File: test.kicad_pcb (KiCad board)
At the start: 2 copper layers, 47 x 92.7 mm, 6 parts, among them J1 Conn_01x32_Female, J2 Conn_01x32_Female, J3 DB9_Male, J4 Conn_01x32_Female, J5 Conn_01x32_Female, U1 MCP2551-I-SN

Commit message: Update db9 position for CAD
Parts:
- J3: moved to B.Cu
- moved J3 22.1 mm to (88.3, 136.0), turned to 180 degrees
- moved J4 11.8 mm to (106.8, 62.2)
- moved J5 11.8 mm to (109.3, 62.2)
- moved U1 6.36 mm to (82.7, 127.2), turned to 180 degrees
- moved J1 2.58 mm to (56.1, 62.2)
- moved J2 2.58 mm to (58.6, 62.2)
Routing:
- net PB12: track 218.9 -> 26.0 mm
- net canH: track 26.8 -> 14.9 mm
- net canL: track 22.6 -> 13.8 mm
- net PB13: track 32.3 -> 24.0 mm
- net GND_STM: track 37.1 -> 40.4 mm
- net +5V_STM: track 79.1 -> 77.7 mm
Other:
- board size 47 x 92.7 mm -> 56.7 x 82.3 mm

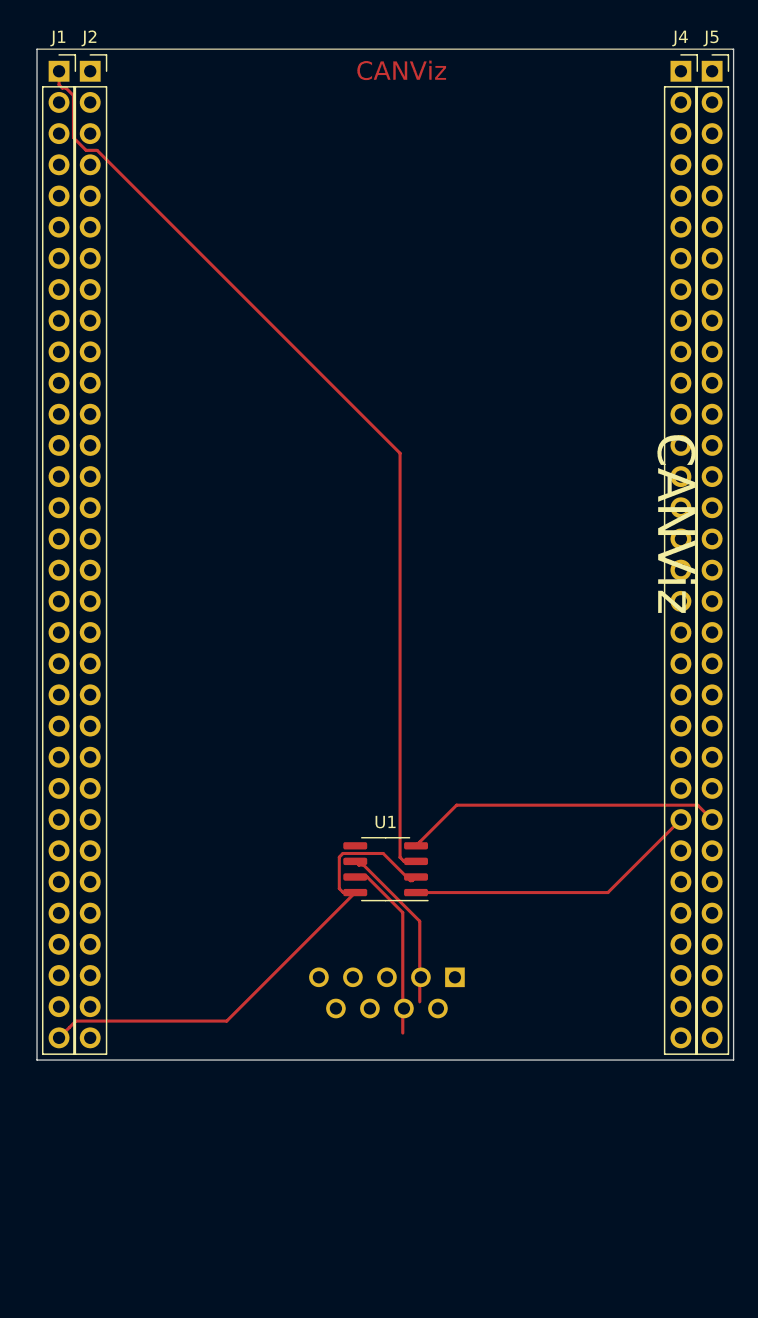
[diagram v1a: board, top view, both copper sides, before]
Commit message: use less pin sockets
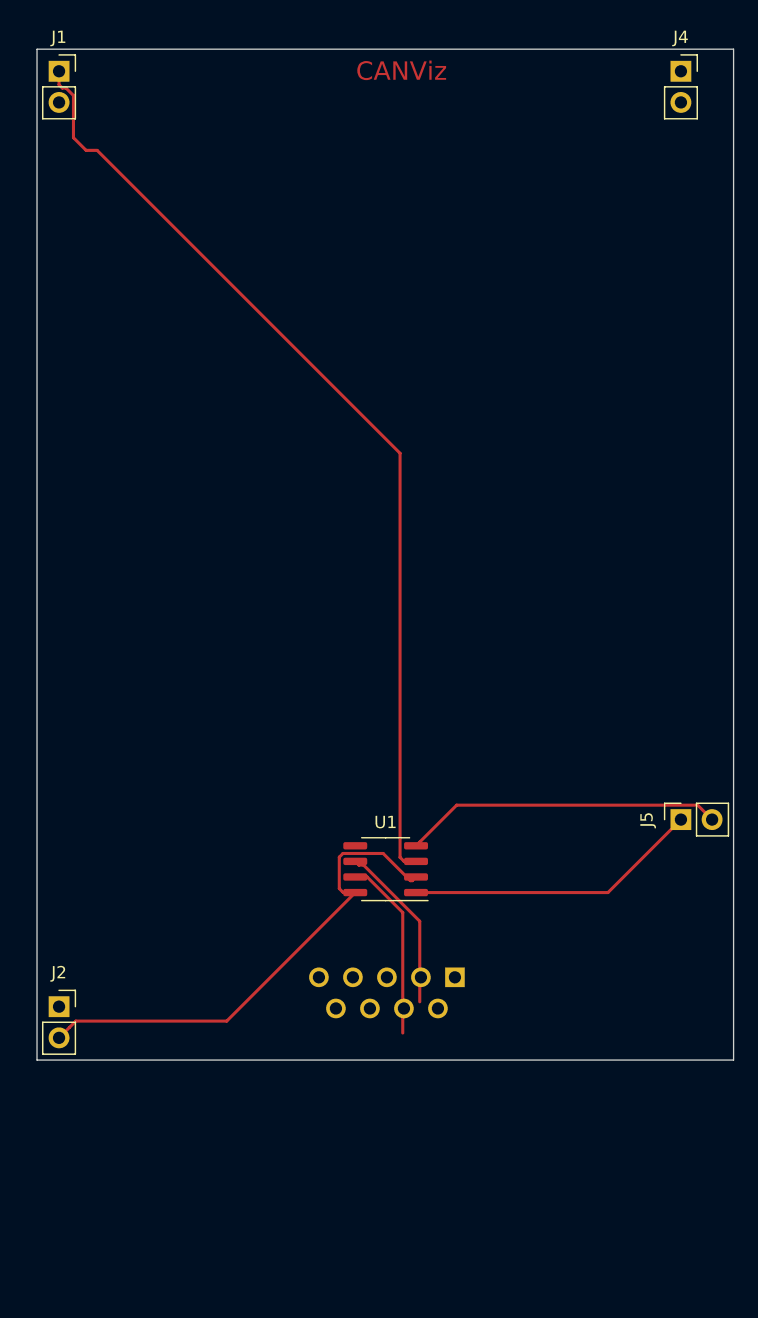
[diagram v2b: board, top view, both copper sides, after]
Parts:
- J1, J2, J4, J5: value Conn_01x32_Female -> Conn_01x02_Female; footprint Connector_PinSocket_2.54mm:PinSocket_1x32_P2.54mm_Vertical -> Connector_PinSocket_2.54mm:PinSocket_1x02_P2.54mm_Vertical
- moved J2 76.2 mm to (56.1, 138.4)
- moved J5 61.0 mm to (106.8, 123.2), turned to 90 degrees
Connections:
- J2 pad 2: Net-(J2-Pad2) -> GND_STM
- J5 pad 1: Net-(J5-Pad1) -> PB13
- J5 pad 2: Net-(J5-Pad2) -> PB12

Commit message: Gerbers and BOM files
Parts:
- moved J4 2.60 mm to (109.4, 62.2)
- moved J5 0.06 mm to (106.8, 123.2)
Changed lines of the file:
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@@
     (thickness 1.6)
     (drawings 7)
-    (tracks 38)
+    (tracks 32)
     (zones 0)
     (modules 6)
@@
       (outputformat 1)
       (mirror false)
-      (drillshape 1)
+      (drillshape 0)
       (scaleselection 1)
-      (outputdirectory ""))
+      (outputdirectory "gerbers/"))
   )
   (net 0 "")
@@
   )
   (module Connector_PinSocket_2.54mm:PinSocket_1x02_P2.54mm_Vertical (layer F.Cu)
-    (at 106.76 62.2)
+    (at 109.36 62.2)
     (descr "Through hole straight socket strip, 1x02, 2.54mm pitch, single row (from Kicad 4.0.7), script generated")
     (tags "Through hole socket strip THT 1x02 2.54mm single row")
@@
   )
   (module Connector_PinSocket_2.54mm:PinSocket_1x02_P2.54mm_Vertical (layer F.Cu)
-    (at 106.76 123.16 90)
+    (at 106.82 123.16 90)
     (descr "Through hole straight socket strip, 1x02, 2.54mm pitch, single row (from Kicad 4.0.7), script generated")
     (tags "Through hole socket strip THT 1x02 2.54mm single row")
@@
   (gr_line (start 111.0488 142.748) (end 111.0488 60.4012) (layer Edge.Cuts) (width 0.05))
   (gr_line (start 54.3052 142.748) (end 111.0488 142.748) (layer Edge.Cuts) (width 0.05))
-  (segment (start 84.2045 126.565) (end 85.1795 126.565) (width 0.25) (layer F.Cu) (net 1))
-  (segment (start 83.87949 126.23999) (end 84.2045 126.565) (width 0.25) (layer F.Cu) (net 1))
-  (segment (start 59.204001 68.644999) (end 83.87949 93.320488) (width 0.25) (layer F.Cu) (net 1))
-  (segment (start 58.307199 68.644999) (end 59.204001 68.644999) (width 0.25) (layer F.Cu) (net 1))
-  (segment (start 57.275001 64.175999) (end 57.275001 67.612801) (width 0.25) (layer F.Cu) (net 1))
-  (segment (start 56.664001 63.564999) (end 57.275001 64.175999) (width 0.25) (layer F.Cu) (net 1))
-  (segment (start 56.364999 63.564999) (end 56.664001 63.564999) (width 0.25) (layer F.Cu) (net 1))
-  (segment (start 57.275001 67.612801) (end 58.307199 68.644999) (width 0.25) (layer F.Cu) (net 1))
-  (segment (start 56.1 63.3) (end 56.364999 63.564999) (width 0.25) (layer F.Cu) (net 1))
-  (segment (start 83.87949 93.320488) (end 83.87949 126.23999) (width 0.25) (layer F.Cu) (net 1))
-  (segment (start 56.1 62.2) (end 56.1 63.3) (width 0.25) (layer F.Cu) (net 1))
+  (segment (start 57.2 62.2) (end 56.1 62.2) (width 0.25) (layer F.Cu) (net 1))
+  (segment (start 57.275001 62.275001) (end 57.2 62.2) (width 0.25) (layer F.Cu) (net 1))
+  (segment (start 57.275001 99.635501) (end 57.275001 62.275001) (width 0.25) (layer F.Cu) (net 1))
+  (segment (start 84.2045 126.565) (end 57.275001 99.635501) (width 0.25) (layer F.Cu) (net 1))
+  (segment (start 85.1795 126.565) (end 84.2045 126.565) (width 0.25) (layer F.Cu) (net 1))
   (segment (start 78.92949 128.77999) (end 79.2545 129.105) (width 0.25) (layer F.Cu) (net 3))
   (segment (start 78.92949 126.218242) (end 78.92949 128.77999) (width 0.25) (layer F.Cu) (net 3))

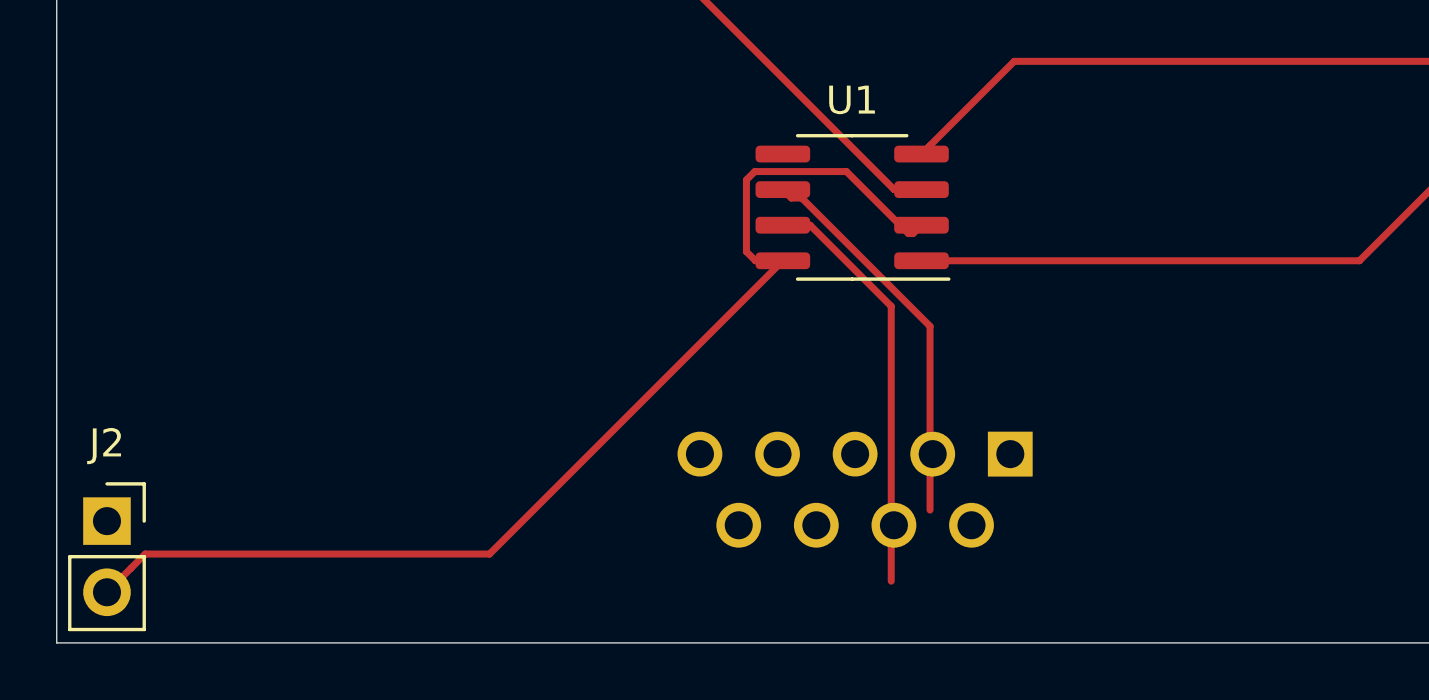
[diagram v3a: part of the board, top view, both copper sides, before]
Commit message: housed db9
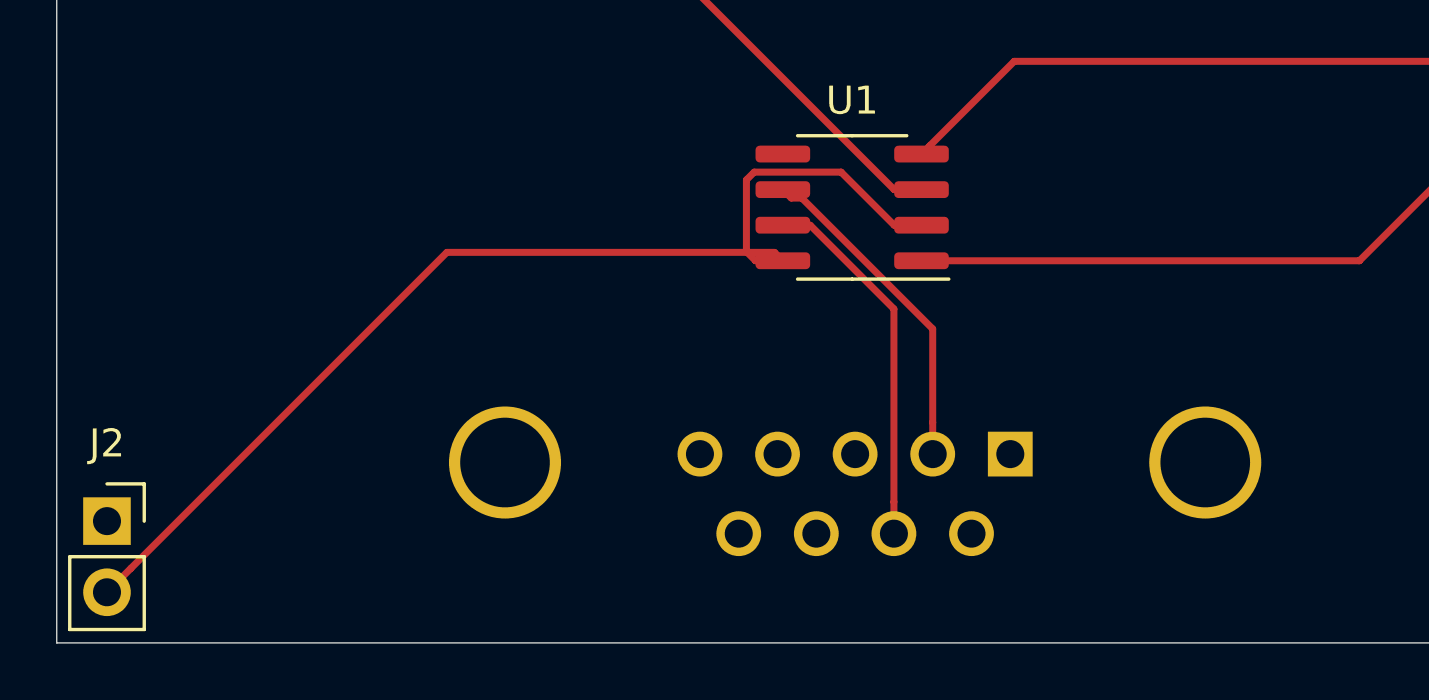
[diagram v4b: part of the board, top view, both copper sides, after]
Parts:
- J3: footprint Connector_Dsub:DSUB-9_Male_Horizontal_P2.77x2.54mm_EdgePinOffset9.40mm -> Connector_Dsub:DSUB-9_Male_Horizontal_P2.77x2.84mm_EdgePinOffset4.94mm_Housed_MountingHolesOffset7.48mm
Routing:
- net canL: track 13.8 -> 11.9 mm
- net canH: track 14.9 -> 13.2 mm

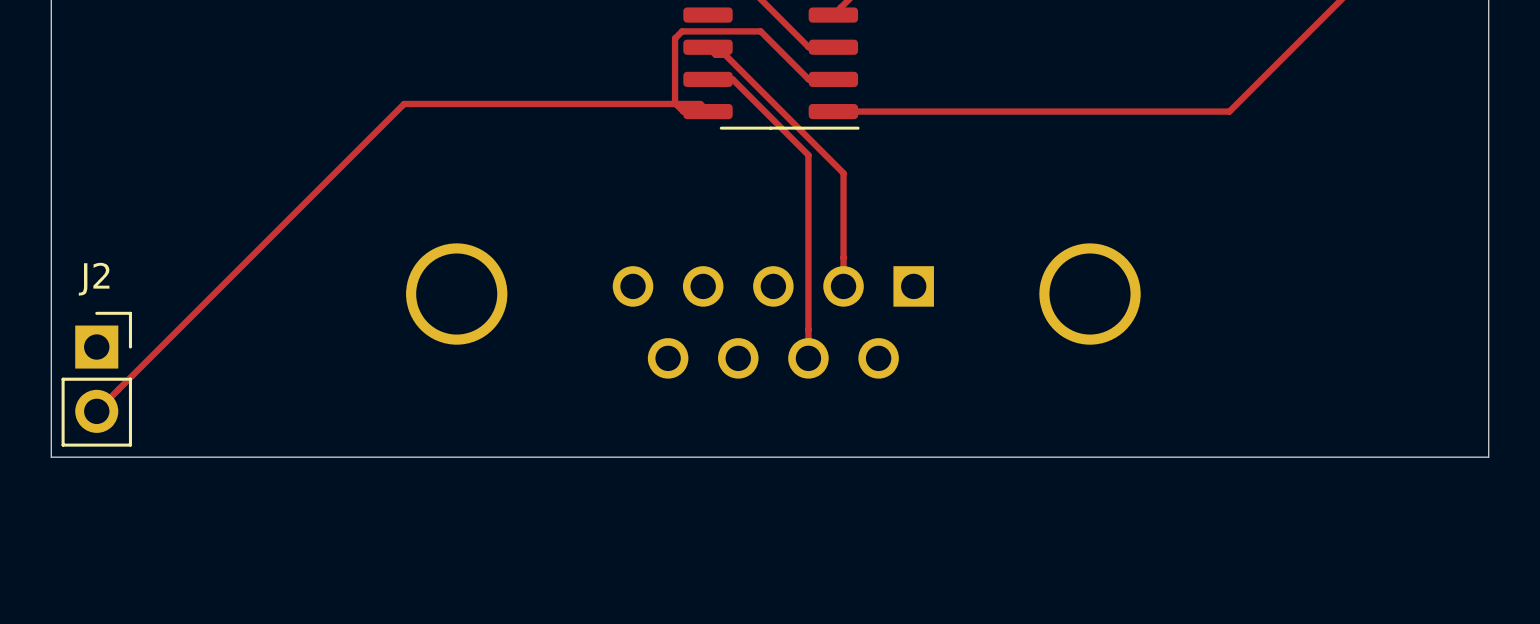
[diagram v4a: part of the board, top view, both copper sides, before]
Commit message: change shape of PCB due to new db9
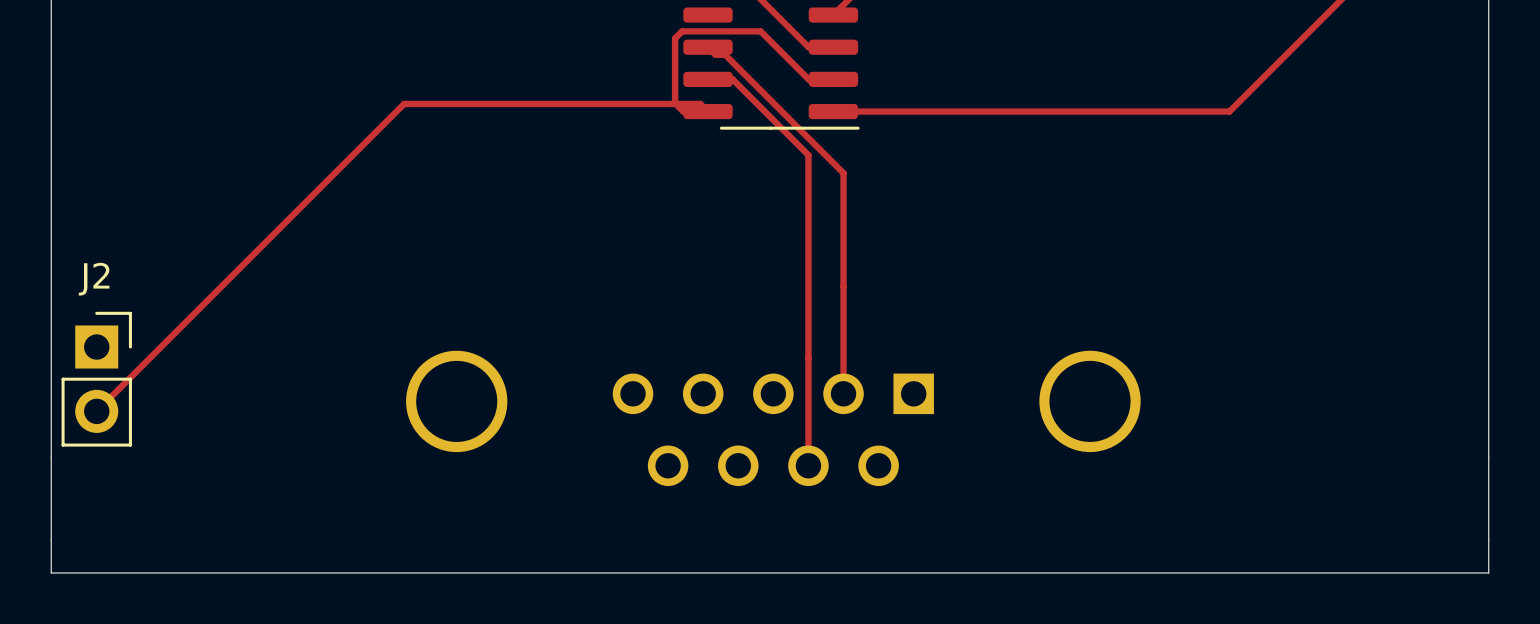
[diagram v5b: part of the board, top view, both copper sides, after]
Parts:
- moved J3 4.24 mm to (88.3, 140.2)
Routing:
- net canL: track 11.9 -> 16.1 mm
- net canH: track 13.2 -> 17.5 mm
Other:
- board size 56.7 x 82.3 mm -> 56.7 x 86.9 mm
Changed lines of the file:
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@@
   (general
     (thickness 1.6)
-    (drawings 7)
+    (drawings 11)
     (tracks 31)
     (zones 0)
@@
   )
   (module Connector_Dsub:DSUB-9_Male_Horizontal_P2.77x2.84mm_EdgePinOffset4.94mm_Housed_MountingHolesOffset7.48mm (layer B.Cu)
-    (at 88.35 136.00758 180)
+    (at 88.35 140.24758 180)
     (descr "9-pin D-Sub connector, horizontal/angled (90 deg), THT-mount, male, pitch 2.77x2.84mm, pin-PCB-offset 4.9399999999999995mm, distance of mounting holes 25mm, distance of mounting holes to PCB edge 7.4799999999999995mm, see https://disti-assets.s3.amazonaws.com/tonar/files/datasheets/16730.pdf")
     (tags "9-pin D-Sub connector horizontal angled 90deg THT male pitch 2.77x2.84mm pin-PCB-offset 4.9399999999999995mm mounting-holes-distance 25mm mounting-hole-offset 25mm")
@@
     )
   )
+  (gr_line (start 111.0488 147.32) (end 54.3052 147.32) (layer Edge.Cuts) (width 0.05))
+  (gr_line (start 111.0488 146.05) (end 111.0488 147.32) (layer Edge.Cuts) (width 0.05))
+  (gr_line (start 54.3052 146.05) (end 54.3052 147.32) (layer Edge.Cuts) (width 0.05))
+  (gr_line (start 111.0488 142.748) (end 111.0488 146.05) (layer Edge.Cuts) (width 0.05))
+  (gr_line (start 54.3052 142.748) (end 54.3052 146.05) (layer Edge.Cuts) (width 0.05))
   (dimension 60.9646 (width 0.12) (layer F.SilkS)
     (gr_text "60.965 mm" (at 115.5954 92.6823 270) (layer F.SilkS)
@@
   (gr_line (start 111.0488 60.4012) (end 54.3052 60.4012) (layer Edge.Cuts) (width 0.05))
   (gr_line (start 111.0488 142.748) (end 111.0488 60.4012) (layer Edge.Cuts) (width 0.05))
-  (gr_line (start 54.3052 142.748) (end 111.0488 142.748) (layer Edge.Cuts) (width 0.05))
   (segment (start 57.2 62.2) (end 56.1 62.2) (width 0.25) (layer F.Cu) (net 1))
   (segment (start 57.275001 62.275001) (end 57.2 62.2) (width 0.25) (layer F.Cu) (net 1))
@@
   (segment (start 79.2545 129.105) (end 78.92949 128.77999) (width 0.25) (layer F.Cu) (net 3))
   (segment (start 80.2295 129.105) (end 79.2545 129.105) (width 0.25) (layer F.Cu) (net 3))
-  (segment (start 85.58 131.538732) (end 85.58 134.87621) (width 0.25) (layer F.Cu) (net 6))
+  (segment (start 85.58 136.00758) (end 85.58 140.24758) (width 0.25) (layer F.Cu) (net 6))
+  (segment (start 85.58 131.538732) (end 85.58 136.00758) (width 0.25) (layer F.Cu) (net 6))
+  (segment (start 80.2295 126.565) (end 80.5295 126.865) (width 0.25) (layer F.Cu) (net 6))
   (segment (start 80.906268 126.865) (end 85.58 131.538732) (width 0.25) (layer F.Cu) (net 6))
-  (segment (start 85.58 134.87621) (end 85.58 136.00758) (width 0.25) (layer F.Cu) (net 6))
   (segment (start 80.5295 126.865) (end 80.906268 126.865) (width 0.25) (layer F.Cu) (net 6))
-  (segment (start 80.2295 126.565) (end 80.5295 126.865) (width 0.25) (layer F.Cu) (net 6))
-  (segment (start 84.195 137.71621) (end 84.195 138.84758) (width 0.25) (layer F.Cu) (net 11))
+  (segment (start 84.195 138.84758) (end 84.195 143.08758) (width 0.25) (layer F.Cu) (net 11))
+  (segment (start 84.195 130.8255) (end 84.195 138.84758) (width 0.25) (layer F.Cu) (net 11))
+  (segment (start 80.2295 127.835) (end 81.2045 127.835) (width 0.25) (layer F.Cu) (net 11))
   (segment (start 81.2045 127.835) (end 84.195 130.8255) (width 0.25) (layer F.Cu) (net 11))
-  (segment (start 84.195 130.8255) (end 84.195 137.71621) (width 0.25) (layer F.Cu) (net 11))
-  (segment (start 80.2295 127.835) (end 81.2045 127.835) (width 0.25) (layer F.Cu) (net 11))
   (segment (start 100.815 129.105) (end 85.1795 129.105) (width 0.25) (layer F.Cu) (net 16))
   (segment (start 106.76 123.16) (end 100.815 129.105) (width 0.25) (layer F.Cu) (net 16))
